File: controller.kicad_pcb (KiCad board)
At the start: 2 copper layers, 118.3 x 38.9 mm, 22 parts, among them J1 Conn_01x16, J2 Conn_01x08, J3 Conn_01x04, SW1 SW_Push, U1 PRTR5V0U2X, U2 AT90USB1286-AU, Y1 16MHz

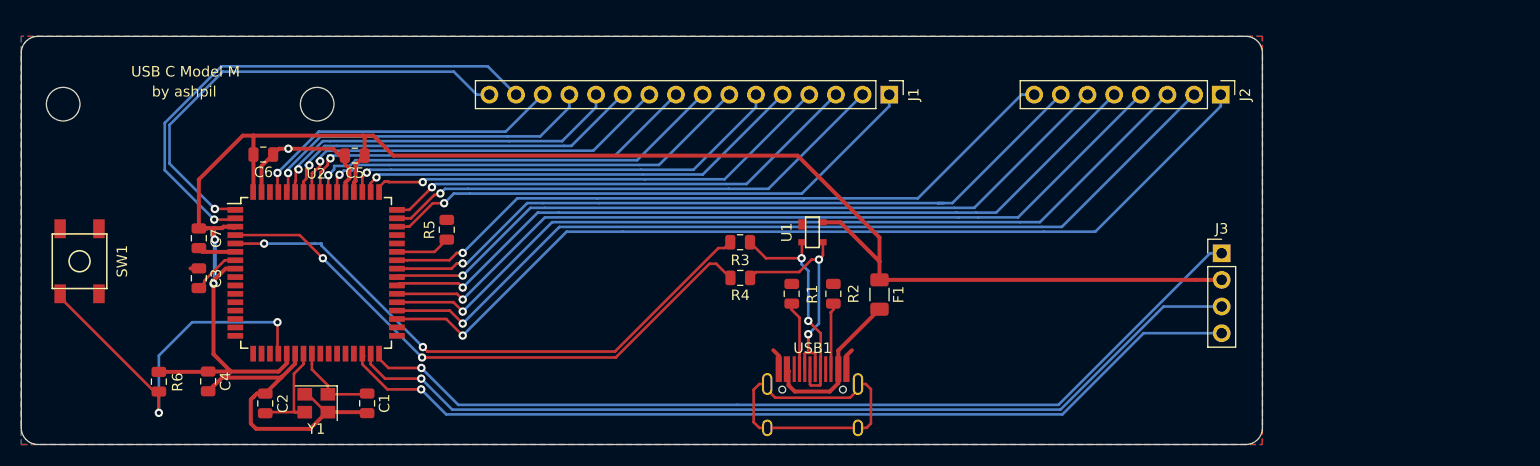
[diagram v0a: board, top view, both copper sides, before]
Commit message: Make it compatible with the M2
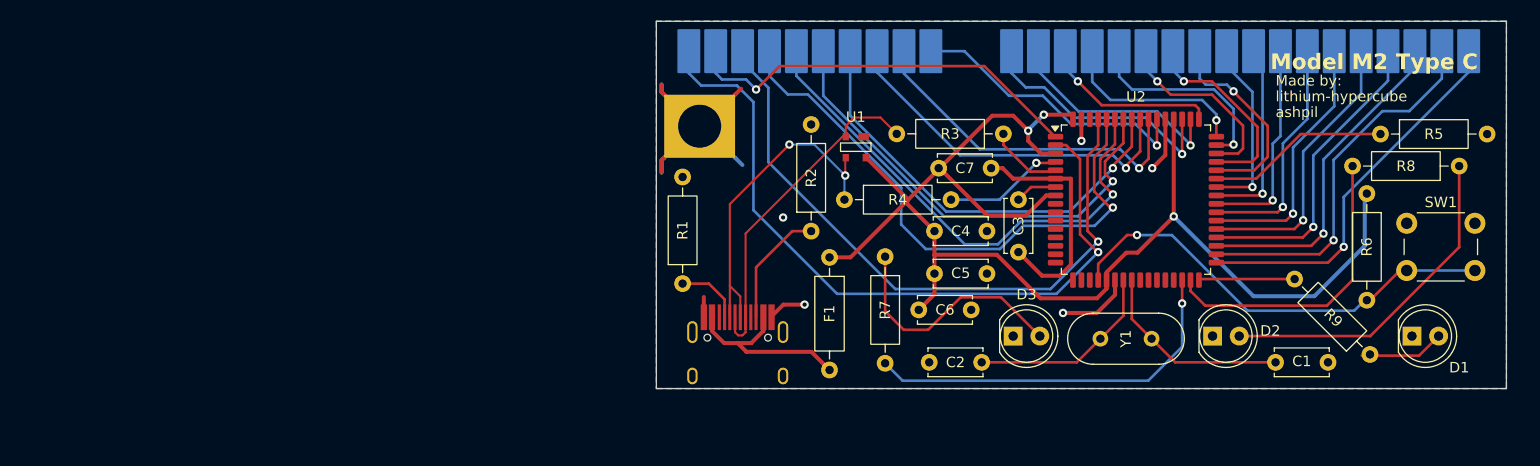
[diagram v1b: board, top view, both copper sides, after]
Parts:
- removed J1: Conn_01x16, Connector_PinHeader_2.54mm:PinHeader_1x16_P2.54mm_Vertical
- removed J2: Conn_01x08, Connector_PinHeader_2.54mm:PinHeader_1x08_P2.54mm_Vertical
- removed J3: Conn_01x04, Connector_PinHeader_2.54mm:PinHeader_1x04_P2.54mm_Vertical
- added 10_exposed_traces1: ~, M2_connectors:10_exposed_traces, F.Cu at (103.0, 70.8)
- added 18_exposed_traces1: ~, M2_connectors:18_exposed_traces, F.Cu at (133.8, 70.8)
- added D1: 3.3v, LED_THT:LED_D5.0mm_IRGrey, F.Cu at (173.0, 100.0)
- added D2: 3.3v, LED_THT:LED_D5.0mm_IRGrey, F.Cu at (154.0, 100.0)
- added D3: 3.3v, LED_THT:LED_D5.0mm_IRGrey, F.Cu at (135.0, 100.0)
- added R7: 270, Resistor_THT:R_Axial_DIN0207_L6.3mm_D2.5mm_P10.16mm_Horizontal, F.Cu at (122.8, 92.4)
- added R8: 270, Resistor_THT:R_Axial_DIN0207_L6.3mm_D2.5mm_P10.16mm_Horizontal, F.Cu at (177.5, 83.8)
- added R9: 270, Resistor_THT:R_Axial_DIN0207_L6.3mm_D2.5mm_P10.16mm_Horizontal, F.Cu at (169.0, 101.8)
- added U3: ~, M2_connectors:screw, F.Cu at (101.8, 77.0)
- C1, C2, C3, C4, C5, C6, C7: footprint Capacitor_SMD:C_0805_2012Metric -> Capacitor_THT:C_Disc_D5.0mm_W2.5mm_P5.00mm
- F1: footprint Fuse:Fuse_1206_3216Metric -> M2_connectors:Littlefuse 0251.500MRT1L
- R1, R2, R3, R4, R5, R6: footprint Resistor_SMD:R_0805_2012Metric -> Resistor_THT:R_Axial_DIN0207_L6.3mm_D2.5mm_P10.16mm_Horizontal
- SW1: footprint random-keyboard-parts:SKQG-1155865 -> Button_Switch_THT:SW_PUSH_6mm_H7.3mm
- U1: footprint random-keyboard-parts:SOT143B -> M2_connectors:SOT143B_silkscreen_compatibility
- Y1: footprint Crystal:Crystal_SMD_3225-4Pin_3.2x2.5mm -> Crystal:Crystal_HC49-U_Vertical
- moved SW1 126.5 mm to (172.5, 89.2), turned to 0 degrees
- moved R6 116.5 mm to (168.7, 86.4)
- moved R5 89.4 mm to (170.0, 80.8), turned to 0 degrees
- moved C1 86.7 mm to (160.0, 102.5), turned to 0 degrees
- moved Y1 79.8 mm to (148.2, 100.2)
- moved C3 78.5 mm to (135.5, 87.0), turned to -90 degrees
- moved U2 78.4 mm to (146.7, 87.0)
- moved C7 70.8 mm to (127.9, 84.0), turned to 0 degrees
- moved C4 70.7 mm to (127.5, 90.0), turned to 0 degrees
- moved C6 64.2 mm to (126.0, 97.5)
- moved C2 63.4 mm to (127.0, 102.5), turned to 0 degrees
- moved C5 56.4 mm to (127.5, 94.0), turned to 0 degrees
- moved R3 27.1 mm to (134.1, 80.7), turned to 180 degrees
- moved R4 12.4 mm to (118.9, 87.0), turned to 0 degrees
- moved R1 10.4 mm to (103.5, 95.0)
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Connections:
- C2 pad 2: Net-(C2-Pad2) -> Net-(U2-XTAL2)
- U2 pad 10: (no net) -> unconnected-(U2-PB0-Pad10)
- U2 pad 11: (no net) -> unconnected-(U2-PB1-Pad11)
- U2 pad 12: (no net) -> unconnected-(U2-PB2-Pad12)
- U2 pad 13: (no net) -> unconnected-(U2-PB3-Pad13)
- U2 pad 14: (no net) -> unconnected-(U2-PB4-Pad14)
- U2 pad 15: (no net) -> unconnected-(U2-PB5-Pad15)
- U2 pad 16: (no net) -> unconnected-(U2-PB6-Pad16)
- U2 pad 17: (no net) -> unconnected-(U2-PB7-Pad17)
- U2 pad 18: (no net) -> unconnected-(U2-PE4-Pad18)
- U2 pad 19: (no net) -> unconnected-(U2-PE5-Pad19)
- U2 pad 23: Net-(C2-Pad2) -> Net-(U2-XTAL2)
- U2 pad 25: (no net) -> unconnected-(U2-PD0-Pad25)
- U2 pad 26: (no net) -> unconnected-(U2-PD1-Pad26)
- U2 pad 27: (no net) -> unconnected-(U2-PD2-Pad27)
- U2 pad 28: (no net) -> unconnected-(U2-PD3-Pad28)
- U2 pad 29: (no net) -> unconnected-(U2-PD4-Pad29)
- U2 pad 33: (no net) -> 10
- U2 pad 34: (no net) -> 9
- U2 pad 44: (no net) -> 1
- U2 pad 45: (no net) -> 2
- U2 pad 46: 1 -> 3
- U2 pad 47: 2 -> 4
- U2 pad 48: 3 -> 5
- U2 pad 49: 4 -> 6
- U2 pad 50: 5 -> 7
- U2 pad 51: 6 -> 8
- U2 pad 62: (no net) -> unconnected-(U2-AREF-Pad62)
- U2 pad 9: (no net) -> unconnected-(U2-PE3-Pad9)
- USB1 pad 13: Net-(USB1-Pad13) -> GND
- USB1 pad 3: (no net) -> unconnected-(USB1-SBU2-Pad3)
- USB1 pad 9: (no net) -> unconnected-(USB1-SBU1-Pad9)
- Y1 pad 2: GND -> Net-(U2-XTAL2)
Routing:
- net Net-(U2-PD7): track 88.6 -> 9.16 mm, vias 1 -> 0
- net Net-(U2-PD6): track 88.0 -> 28.9 mm, vias 1 -> 0
- net Net-(U2-PC0): track 89.3 -> 31.7 mm
- net Net-(U2-PC1): track 85.5 -> 29.4 mm
- net Net-(U2-PC2): track 82.4 -> 27.0 mm
- net Net-(U2-PC3): track 79.3 -> 24.7 mm
- net Net-(U2-PC4): track 76.3 -> 22.4 mm
- net Net-(U2-PC5): track 73.0 -> 20.0 mm
- net Net-(U2-PC6): track 70.7 -> 18.5 mm
- net Net-(U2-PD5): track 88.4 -> 36.6 mm
- net Net-(U2-PC7): track 67.3 -> 17.4 mm
- net Net-(U2-D+): track 55.9 -> 6.82 mm, vias 2 -> 0
- net Net-(U2-D-): track 56.3 -> 11.4 mm, vias 2 -> 1
- net 10: track 0.00 -> 36.3 mm, vias 0 -> 1
- net 9: track 0.00 -> 35.5 mm, vias 0 -> 1
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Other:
- board size 118.3 x 38.9 mm -> 81 x 35 mm
- net class Default removed
- net class Power removed
- rule pad_to_mask_clearance: 0.051 -> 0
- board text added: "Made by:"
- board text added: "Model M2 Type C"
- board text added: "ashpil"
- board text added: "lithium-hypercube"
- board text removed: "USB C Model M"
- board text removed: "by ashpil"
